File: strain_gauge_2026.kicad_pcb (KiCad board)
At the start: 2 copper layers, 82 x 42 mm, 26 parts, among them J3 Conn_01x04_Socket, J5 Conn_01x04_Socket, U1 NAU7802SGI

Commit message: removed a small floating trace between pins 7 and 8 on U2
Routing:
- net +3V3: track 55.9 -> 55.3 mm
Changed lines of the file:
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@@
+	)
+	(segment
+		(start 144.94 111.76)
+		(end 142.9 111.76)
+		(width 0.5)
+		(layer "B.Cu")
+		(net "Net-(U1-VIN2N)")
+	)
+	(segment
+		(start 153.78 97.22)
+		(end 150.7 100.3)
+		(width 0.5)
+		(layer "B.Cu")
+		(net "Net-(U1-VIN2N)")
+	)
+	(segment
+		(start 142.9 113.7)
+		(end 143.9 114.7)
+		(width 0.5)
+		(layer "B.Cu")
+		(net "Net-(U1-VIN2N)")
+	)
+	(segment
+		(start 142.9 111.78)
+		(end 142.9 113.7)
+		(width 0.5)
+		(layer "B.Cu")
+		(net "Net-(U1-VIN2N)")
+	)
+	(segment
+		(start 150.7 106)
+		(end 144.94 111.76)
+		(width 0.5)
+		(layer "B.Cu")
+		(net "Net-(U1-VIN2N)")
+	)
+	(segment
+		(start 150.7 100.3)
+		(end 150.7 106)
+		(width 0.5)
+		(layer "B.Cu")
+		(net "Net-(U1-VIN2N)")
+	)
+	(segment
+		(start 137.06 106.1)
+		(end 142.47 106.1)
+		(width 0.5)
+		(layer "B.Cu")
+		(net "B+")
+	)
+	(segment
+		(start 121.4 107.6)
+		(end 126.2 112.4)
+		(width 0.5)
+		(layer "B.Cu")
+		(net "B+")
+	)
+	(segment
+		(start 126.2 112.4)
+		(end 130.76 112.4)
+		(width 0.5)
+		(layer "B.Cu")
+		(net "B+")
+	)
+	(segment
+		(start 142.47 106.1)
+		(end 146.95 101.62)
+		(width 0.5)
+		(layer "B.Cu")
+		(net "B+")
+	)
+	(segment
+		(start 130.76 112.4)
+		(end 137.06 106.1)
+		(width 0.5)
+		(layer "B.Cu")
+		(net "B+")
+	)
+	(segment
+		(start 121.4 107.46)
+		(end 121.4 107.6)
+		(width 0.2)
+		(layer "B.Cu")
+		(net "B+")
+	)
+	(segment
+		(start 121.4 104.92)
+		(end 121.4 107.46)
+		(width 0.5)
+		(layer "B.Cu")
+		(net "B+")
+	)
+	(segment
+		(start 151.75 106.95)
+		(end 146.95 111.75)
+		(width 0.5)
+		(layer "B.Cu")
+		(net "Net-(U1-VIN2P)")
+	)
+	(segment
+		(start 153.78 99.76)
+		(end 151.75 101.79)
+		(width 0.5)
+		(layer "B.Cu")
+		(net "Net-(U1-VIN2P)")
+	)
+	(segment
+		(start 146.95 111.78)
+		(end 146.95 113.725)
+		(width 0.5)
+		(layer "B.Cu")
+		(net "Net-(U1-VIN2P)")
+	)
+	(segment
+		(start 151.75 101.79)
+		(end 151.75 106.95)
+		(width 0.5)
+		(layer "B.Cu")
+		(net "Net-(U1-VIN2P)")
+	)
+	(segment
+		(start 146.95 111.75)
+		(end 146.95 111.76)
+		(width 0.2)
+		(layer "B.Cu")
+		(net "Net-(U1-VIN2P)")
+	)
+	(segment
+		(start 146.95 113.725)
+		(end 145.975 114.7)
+		(width 0.5)
+		(layer "B.Cu")
+		(net "Net-(U1-VIN2P)")
+	)
+	(segment
+		(start 143 96.35)
+		(end 143.9 97.25)
+		(width 0.5)
+		(layer "B.Cu")
+		(net "Net-(U1-VIN1N)")
+	)
+	(segment
+		(start 145.63 91.4)
+		(end 153.04 91.4)
+		(width 0.5)
+		(layer "B.Cu")
+		(net "Net-(U1-VIN1N)")
+	)
+	(segment
+		(start 143 94.03)
+		(end 143 96.35)
+		(width 0.5)
+		(layer "B.Cu")
+		(net "Net-(U1-VIN1N)")
+	)
+	(segment
+		(start 143 94.03)
+		(end 145.63 91.4)
+		(width 0.5)
+		(layer "B.Cu")
+		(net "Net-(U1-VIN1N)")
+	)
+	(segment
+		(start 153.04 91.4)
+		(end 153.78 92.14)
+		(width 0.5)
+		(layer "B.Cu")
+		(net "Net-(U1-VIN1N)")
 	)
 	(segment
@@
 		(layer "B.Cu")
 		(net "Net-(U1-VIN1P)")
-	)
-	(segment
-		(start 143 96.35)
-		(end 143.9 97.25)
-		(width 0.5)
-		(layer "B.Cu")
-		(net "Net-(U1-VIN1N)")
-	)
-	(segment
-		(start 145.63 91.4)
-		(end 153.04 91.4)
-		(width 0.5)
-		(layer "B.Cu")
-		(net "Net-(U1-VIN1N)")
-	)
-	(segment
-		(start 143 94.03)
-		(end 143 96.35)
-		(width 0.5)
-		(layer "B.Cu")
-		(net "Net-(U1-VIN1N)")
-	)
-	(segment
-		(start 143 94.03)
-		(end 145.63 91.4)
-		(width 0.5)
-		(layer "B.Cu")
-		(net "Net-(U1-VIN1N)")
-	)
-	(segment
-		(start 153.04 91.4)
-		(end 153.78 92.14)
-		(width 0.5)
-		(layer "B.Cu")
-		(net "Net-(U1-VIN1N)")
 	)
 	(segment
@@
 	)
 	(segment
-		(start 151.75 106.95)
-		(end 146.95 111.75)
-		(width 0.5)
-		(layer "B.Cu")
-		(net "Net-(U1-VIN2P)")
-	)
-	(segment
-		(start 153.78 99.76)
-		(end 151.75 101.79)
-		(width 0.5)
-		(layer "B.Cu")
-		(net "Net-(U1-VIN2P)")
-	)
-	(segment
-		(start 146.95 111.78)
-		(end 146.95 113.725)
-		(width 0.5)
-		(layer "B.Cu")
-		(net "Net-(U1-VIN2P)")
-	)
-	(segment
-		(start 151.75 101.79)
-		(end 151.75 106.95)
-		(width 0.5)
-		(layer "B.Cu")
-		(net "Net-(U1-VIN2P)")
-	)
-	(segment
-		(start 146.95 111.75)
-		(end 146.95 111.76)
-		(width 0.2)
-		(layer "B.Cu")
-		(net "Net-(U1-VIN2P)")
-	)
-	(segment
-		(start 146.95 113.725)
-		(end 145.975 114.7)
-		(width 0.5)
-		(layer "B.Cu")
-		(net "Net-(U1-VIN2P)")
-	)
-	(segment
-		(start 144.94 111.76)
-		(end 142.9 111.76)
-		(width 0.5)
-		(layer "B.Cu")
-		(net "Net-(U1-VIN2N)")
-	)
-	(segment
-		(start 153.78 97.22)
-		(end 150.7 100.3)
-		(width 0.5)
-		(layer "B.Cu")
-		(net "Net-(U1-VIN2N)")
-	)
-	(segment
-		(start 142.9 113.7)
-		(end 143.9 114.7)
-		(width 0.5)
-		(layer "B.Cu")
-		(net "Net-(U1-VIN2N)")
-	)
-	(segment
-		(start 142.9 111.78)
-		(end 142.9 113.7)
-		(width 0.5)
-		(layer "B.Cu")
-		(net "Net-(U1-VIN2N)")
-	)
-	(segment
-		(start 150.7 106)
-		(end 144.94 111.76)
-		(width 0.5)
-		(layer "B.Cu")
-		(net "Net-(U1-VIN2N)")
-	)
-	(segment
-		(start 150.7 100.3)
-		(end 150.7 106)
-		(width 0.5)
-		(layer "B.Cu")
-		(net "Net-(U1-VIN2N)")
-	)
-	(segment
-		(start 179.618 89.475)
-		(end 180.017 89.874)
-		(width 0.5)
-		(layer "B.Cu")
-		(net "+3V3")
+		(start 172.607 97.22)
+		(end 182.363 106.976)
+		(width 0.4)
+		(layer "B.Cu")
+		(net "SCLK")
+	)
+	(segment
+		(start 161.4 97.22)
+		(end 172.607 97.22)
+		(width 0.4)
+		(layer "B.Cu")
+		(net "SCLK")
+	)
+	(segment
+		(start 161.4 94.68)
+		(end 172.607 94.68)
+		(width 0.4)
+		(layer "B.Cu")
+		(net "SDA")
+	)
+	(segment
+		(start 172.607 94.68)
+		(end 184.903 106.976)
+		(width 0.4)
+		(layer "B.Cu")
+		(net "SDA")
 	)
 	(segment
@@
 		(net "+3V3")
 	)
-	(segment
-		(start 137.06 106.1)
-		(end 142.47 106.1)
-		(width 0.5)
-		(layer "B.Cu")
-		(net "B+")
-	)
-	(segment
-		(start 121.4 107.6)
-		(end 126.2 112.4)
-		(width 0.5)
-		(layer "B.Cu")
-		(net "B+")
-	)
-	(segment
-		(start 126.2 112.4)
-		(end 130.76 112.4)
-		(width 0.5)
-		(layer "B.Cu")
-		(net "B+")
-	)
-	(segment
-		(start 142.47 106.1)
-		(end 146.95 101.62)
-		(width 0.5)
-		(layer "B.Cu")
-		(net "B+")
-	)
-	(segment
-		(start 130.76 112.4)
-		(end 137.06 106.1)
-		(width 0.5)
-		(layer "B.Cu")
-		(net "B+")
-	)
-	(segment
-		(start 121.4 107.46)
-		(end 121.4 107.6)
-		(width 0.2)
-		(layer "B.Cu")
-		(net "B+")
-	)
-	(segment
-		(start 121.4 104.92)
-		(end 121.4 107.46)
-		(width 0.5)
-		(layer "B.Cu")
-		(net "B+")
-	)
-	(segment
-		(start 172.607 97.22)
-		(end 182.363 106.976)
-		(width 0.4)
-		(layer "B.Cu")
-		(net "SCLK")
-	)
-	(segment
-		(start 161.4 97.22)
-		(end 172.607 97.22)
-		(width 0.4)
-		(layer "B.Cu")
-		(net "SCLK")
-	)
-	(segment
-		(start 161.4 94.68)
-		(end 172.607 94.68)
-		(width 0.4)
-		(layer "B.Cu")
-		(net "SDA")
-	)
-	(segment
-		(start 172.607 94.68)
-		(end 184.903 106.976)
-		(width 0.4)
-		(layer "B.Cu")
-		(net "SDA")
-	)
 	(zone

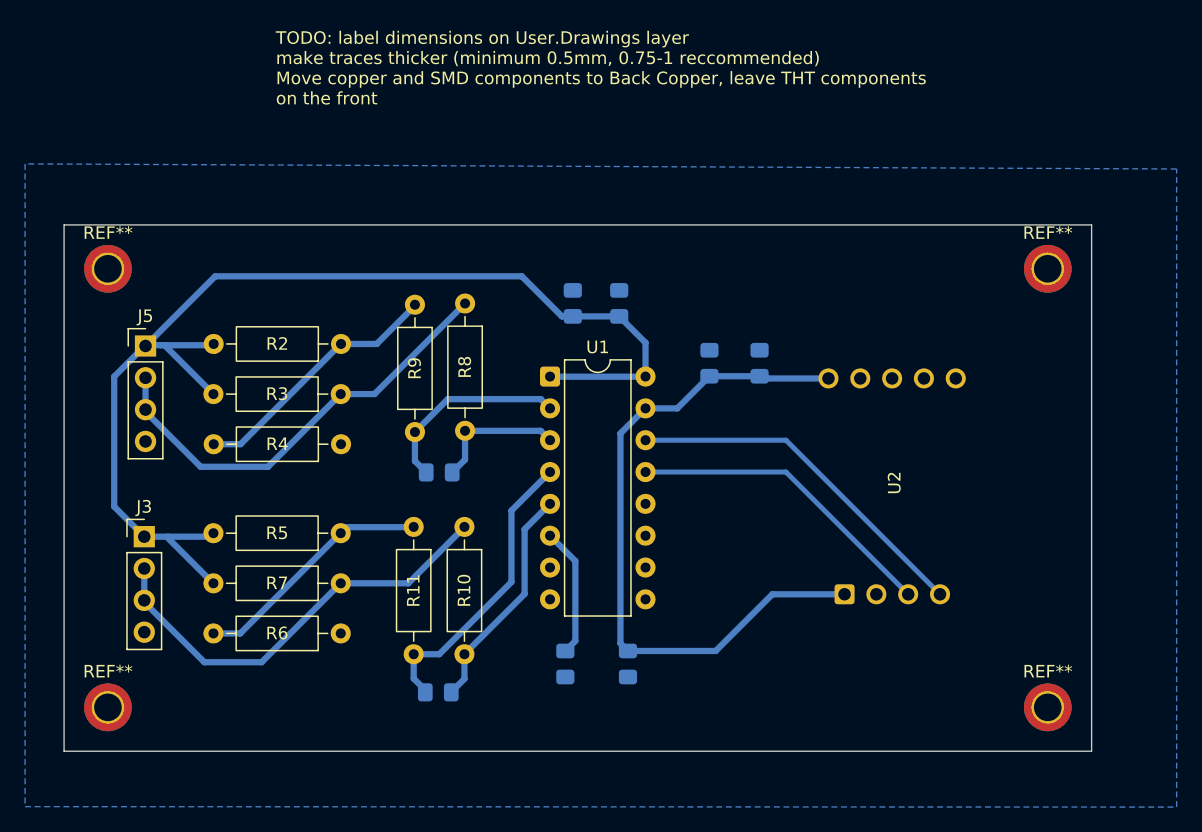
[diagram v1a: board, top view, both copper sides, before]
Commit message: Moved some things around to make the board smaller
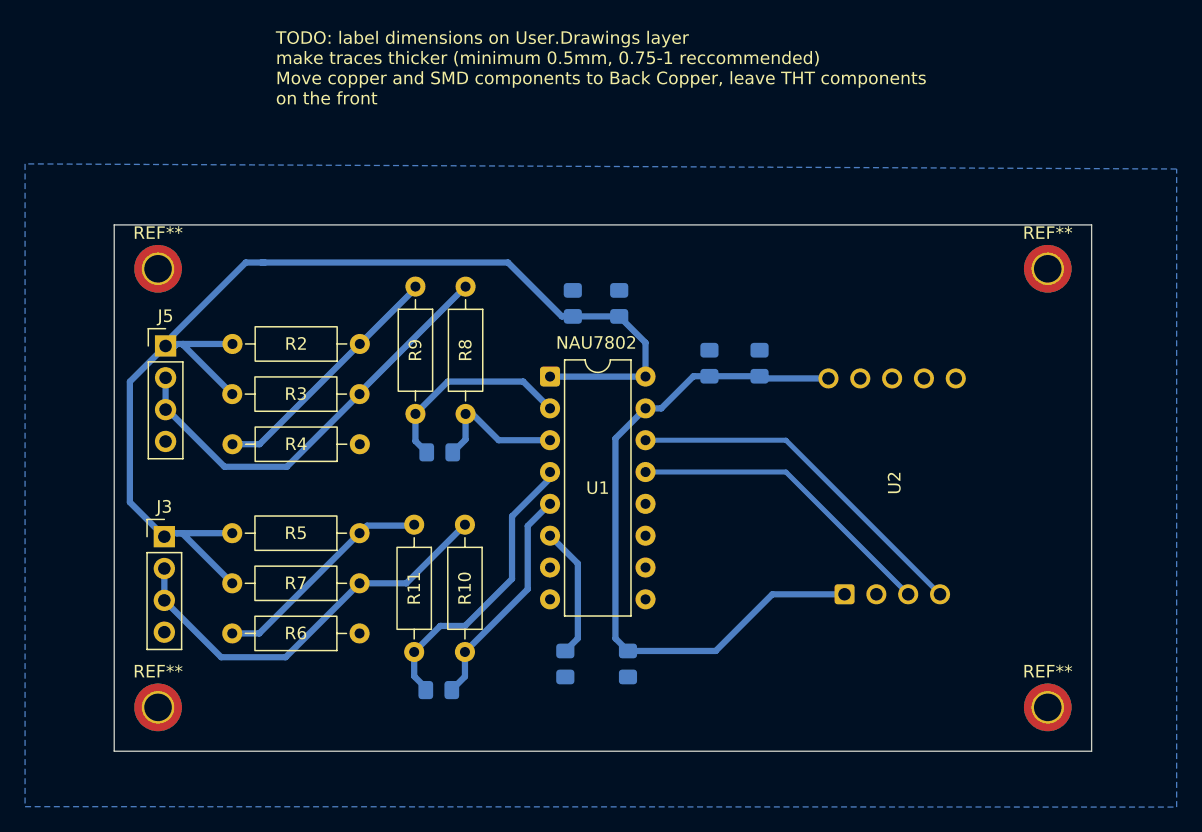
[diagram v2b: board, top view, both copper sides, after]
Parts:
- moved REF** 4.00 mm to (122.5, 116.0)
- moved REF** 4.00 mm to (122.5, 81.0)
- moved C2 1.60 mm to (145.0, 95.7)
- moved J3 1.60 mm to (123.0, 102.4)
- moved J5 1.60 mm to (123.1, 87.2)
- moved R2 1.50 mm to (138.6, 87.0)
- moved R3 1.50 mm to (138.6, 91.0)
- moved R4 1.50 mm to (138.6, 95.0)
- moved R5 1.50 mm to (138.6, 102.1)
- moved R6 1.50 mm to (138.6, 110.1)
- moved R7 1.50 mm to (138.6, 106.1)
- moved R9 1.45 mm to (143.0, 82.4)
- moved R8 1.35 mm to (147.0, 82.4)
- moved R10 0.18 mm to (147.0, 101.4)
- moved C3 0.18 mm to (144.9, 114.6)
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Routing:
- net V_excitation: track 94.0 -> 95.6 mm
- net B+: track 34.7 -> 33.2 mm
- net B-: track 19.5 -> 18.1 mm
- net A+: track 35.5 -> 34.5 mm
- net A-: track 20.7 -> 20.0 mm
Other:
- board size 82 x 42 mm -> 78 x 42 mm
- board text added: "NAU7802"

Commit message: Changed 2x4pin JST connectors for strain resistors to 4x2pin connectors
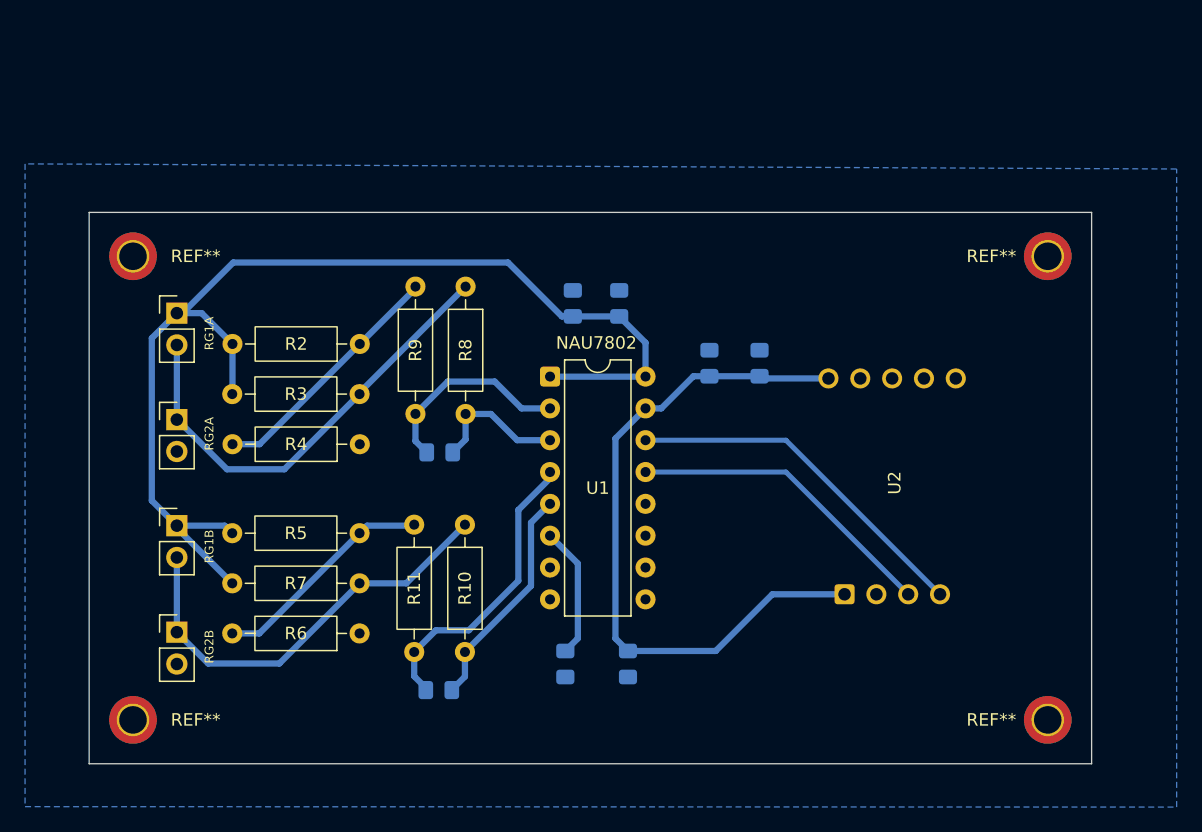
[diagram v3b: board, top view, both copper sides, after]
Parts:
- removed J5: Conn_01x04_Socket, Connector_PinHeader_2.54mm:PinHeader_1x04_P2.54mm_Vertical
- added J1: Conn_01x02_Socket, Connector_PinHeader_2.54mm:PinHeader_1x02_P2.54mm_Vertical, F.Cu at (124.0, 84.5)
- added J2: Conn_01x02_Socket, Connector_PinHeader_2.54mm:PinHeader_1x02_P2.54mm_Vertical, F.Cu at (124.0, 93.0)
- added J4: Conn_01x02_Socket, Connector_PinHeader_2.54mm:PinHeader_1x02_P2.54mm_Vertical, F.Cu at (124.0, 110.0)
- J3: value Conn_01x04_Socket -> Conn_01x02_Socket; footprint Connector_PinHeader_2.54mm:PinHeader_1x04_P2.54mm_Vertical -> Connector_PinHeader_2.54mm:PinHeader_1x02_P2.54mm_Vertical
- moved REF** 2.24 mm to (120.5, 117.0)
- moved REF** 2.24 mm to (120.5, 80.0)
- moved J3 1.33 mm to (124.0, 101.5)
- moved REF** 1.00 mm to (193.5, 117.0)
- moved REF** 1.00 mm to (193.5, 80.0)
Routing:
- net V_excitation: track 95.6 -> 92.5 mm
- net B+: track 33.2 -> 35.0 mm
- net A+: track 34.5 -> 36.2 mm
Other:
- board size 78 x 42 mm -> 80 x 44 mm
- board text added: "RG1A"
- board text added: "RG1B"
- board text added: "RG2A"
- board text added: "RG2B"
- board text removed: "TODO: label dimensions on User.Drawings layer make traces thicker (minimum 0.5mm, 0.75-1 reccommended) Move copper and SMD components to Back Copper, leave THT components on the front"
